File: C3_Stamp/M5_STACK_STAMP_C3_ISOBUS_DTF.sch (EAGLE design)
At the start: 13 parts, among them IC1 MCP2562-E_P, J1 61300811121, J2 61300611121, J3 DTF13-4P

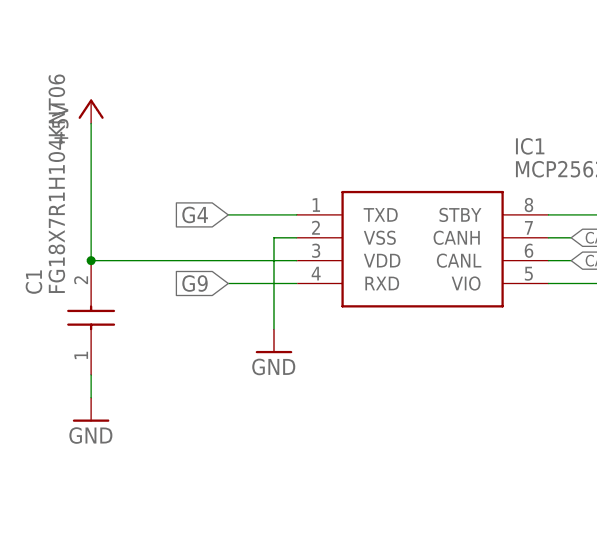
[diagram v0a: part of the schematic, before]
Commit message: G7 for CAN RX, as G9 is a Strapping Pin.
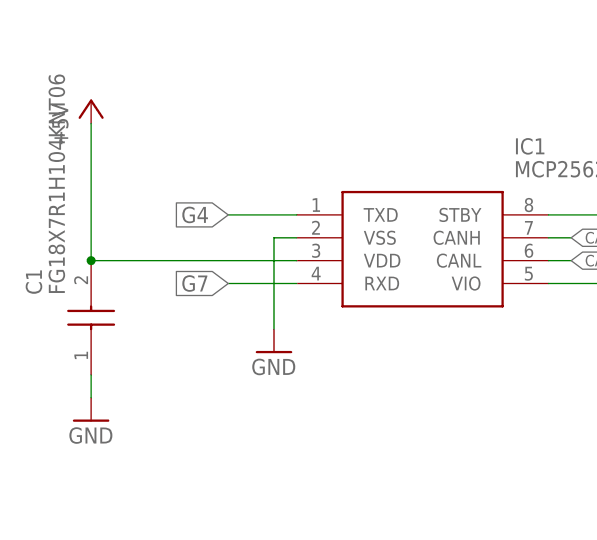
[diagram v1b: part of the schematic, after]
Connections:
- net G7: now also IC1.RXD
- net G9: no longer IC1.RXD
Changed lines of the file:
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@@
 <label x="25.4" y="86.36" size="1.27" layer="95" xref="yes"/>
-</segment>
-<segment>
-<pinref part="IC1" gate="G$1" pin="RXD"/>
-<wire x1="2.54" y1="25.4" x2="-5.08" y2="25.4" width="0.1524" layer="91"/>
-<label x="-5.08" y="25.4" size="1.778" layer="95" rot="R180" xref="yes"/>
 </segment>
 </net>
@@
 <label x="-5.08" y="91.44" size="1.27" layer="95" rot="R180" xref="yes"/>
 </segment>
+<segment>
+<pinref part="IC1" gate="G$1" pin="RXD"/>
+<wire x1="2.54" y1="25.4" x2="-5.08" y2="25.4" width="0.1524" layer="91"/>
+<label x="-5.08" y="25.4" size="1.778" layer="95" rot="R180" xref="yes"/>
+</segment>
 </net>
